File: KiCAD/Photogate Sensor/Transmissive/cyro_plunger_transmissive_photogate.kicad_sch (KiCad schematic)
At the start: 60 parts, among them J1 FFC, J2 FFC Socket, J3 USB_B_Micro, J4 UPDI socket, J5 DC Jack, J6 Conn_01x03_Socket, J7 USB_B_Micro, J8 FFC Socket, J9 Conn_01x03_Socket, Q1 Q_NMOS_GSD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

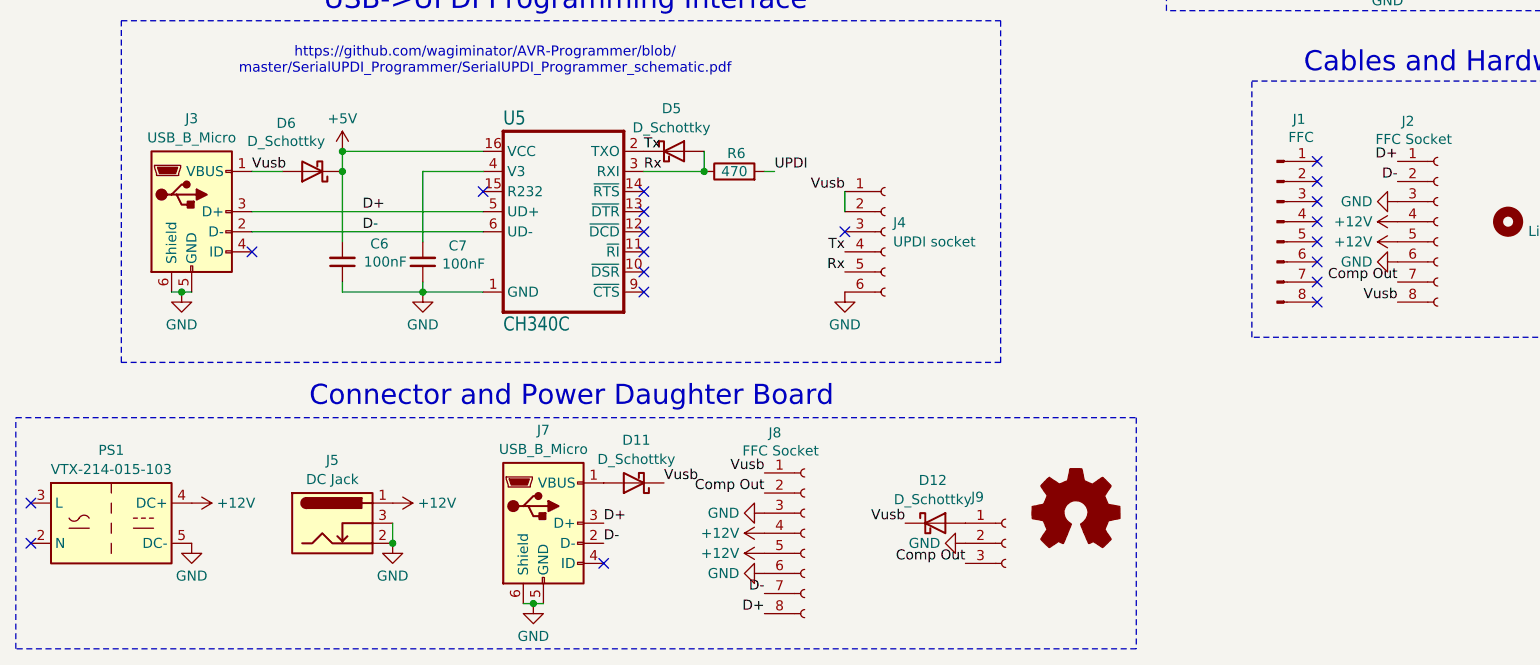
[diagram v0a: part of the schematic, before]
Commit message: Remove second USB connector
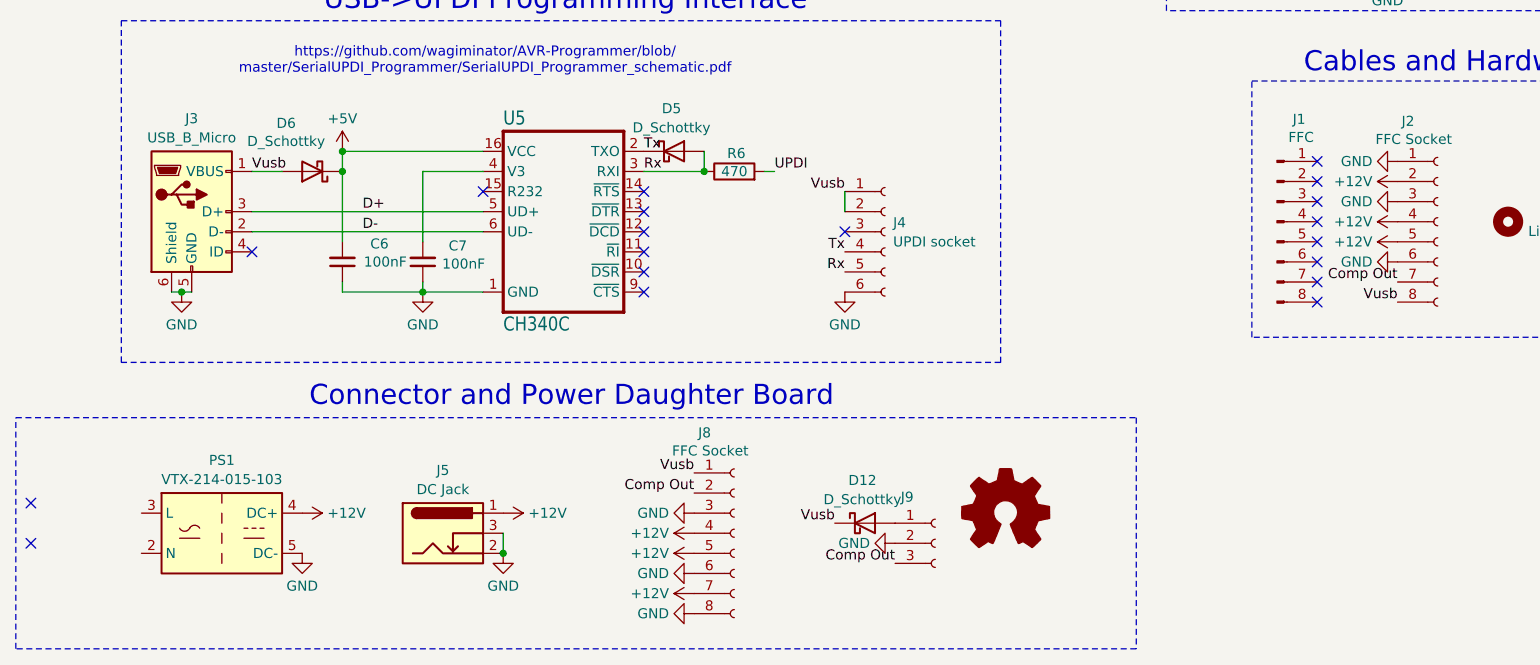
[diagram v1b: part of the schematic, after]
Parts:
- removed D11: D_Schottky, Diode_SMD:D_SOD-323, symbol Device:D_Schottky
- removed J7: USB_B_Micro, Custom:CUI_UJ2-MIBH-G-SMT-TR, symbol Connector:USB_B_Micro
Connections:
- net +12V: now also J2.2 (Pin_2), J8.7 (Pin_7)
- net D+: no longer J2.1 (Pin_1), J8.8 (Pin_8)
- net D-: no longer J2.2 (Pin_2), J8.7 (Pin_7)
- net GND: now also J2.1 (Pin_1), J8.8 (Pin_8)
- no-connect marks 26 -> 25
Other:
- moved on the sheet: D12, J5, J8, J9, PS1
